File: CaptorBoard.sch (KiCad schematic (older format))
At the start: 55 parts, among them CON1 MINI-USB-SHELD-MC32598, P1 Prog, P2 POWER, P3 EXT, Q1 IRLM6402TRPBF, SW1 CST06S08H, U1 PIC32MX795F512H-80I-PT, U2 MRF24J40MA-I-RM, U3 HTU21, U4 MPL115A2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

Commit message: Forgot foot print
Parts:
- U5: footprint pfo:VTX-214-003-105 -> pfo:VTX-214-005-x
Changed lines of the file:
@@
 F 0 "U5" H 9450 10000 50  0000 C CNN
 F 1 "VTX-214-003-105" H 9750 9400 50  0000 C CNN
-F 2 "pfo:VTX-214-003-105" H 10150 9400 50  0001 C CNN
+F 2 "pfo:VTX-214-005-x" H 10150 9400 50  0001 C CNN
 F 3 "DOCUMENTATION" H 10000 10000 50  0001 C CNN
 	1    9850 9700

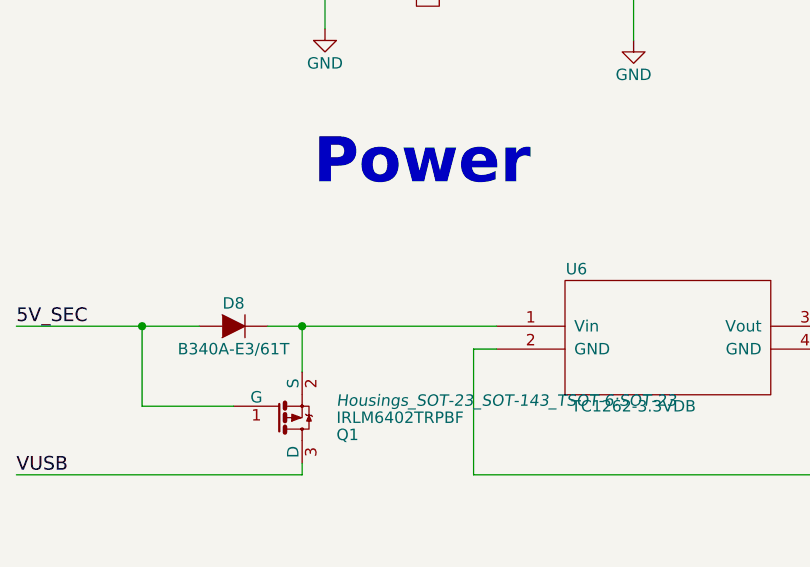
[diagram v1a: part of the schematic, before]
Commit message: Add marker for 5V
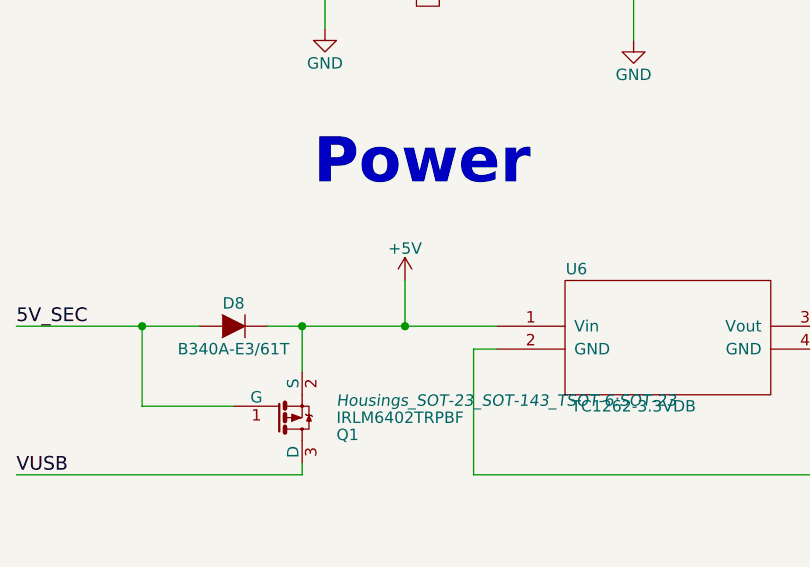
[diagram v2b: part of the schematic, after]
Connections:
- net labels added: +5V
- wire segments 218 -> 219
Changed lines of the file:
@@
 Text Label 12700 7650 0    60   ~ 0
 Phase_F
+$Comp
+L +5V #PWR?
+U 1 1 55364DDB
+P 9600 7750
+F 0 "#PWR?" H 9600 7600 50  0001 C CNN
+F 1 "+5V" H 9600 7890 50  0000 C CNN
+F 2 "" H 9600 7750 60  0000 C CNN
+F 3 "" H 9600 7750 60  0000 C CNN
+	1    9600 7750
+	1    0    0    -1
+$EndComp
+Wire Wire Line
+	9600 7750 9600 7950
+Connection ~ 9600 7950
 $EndSCHEMATC

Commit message: Change HST21
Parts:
- U3: footprint Housings_DFN_QFN:DFN-6-1EP_3x3mm_Pitch0.95mm -> pfo:HTU21
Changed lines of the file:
@@
 F 0 "U3" H 1950 9650 50  0000 C CNN
 F 1 "HTU21" H 2000 9050 50  0000 C CNN
-F 2 "Housings_DFN_QFN:DFN-6-1EP_3x3mm_Pitch0.95mm" H 2650 9050 50  0001 C CNN
+F 2 "pfo:HTU21" H 2650 9050 50  0001 C CNN
 F 3 "DOCUMENTATION" H 2500 9650 50  0001 C CNN
 	1    2350 9350
@@
 Phase_F
 $Comp
-L +5V #PWR?
+L +5V #PWR033
 U 1 1 55364DDB
 P 9600 7750
-F 0 "#PWR?" H 9600 7600 50  0001 C CNN
+F 0 "#PWR033" H 9600 7600 50  0001 C CNN
 F 1 "+5V" H 9600 7890 50  0000 C CNN
 F 2 "" H 9600 7750 60  0000 C CNN

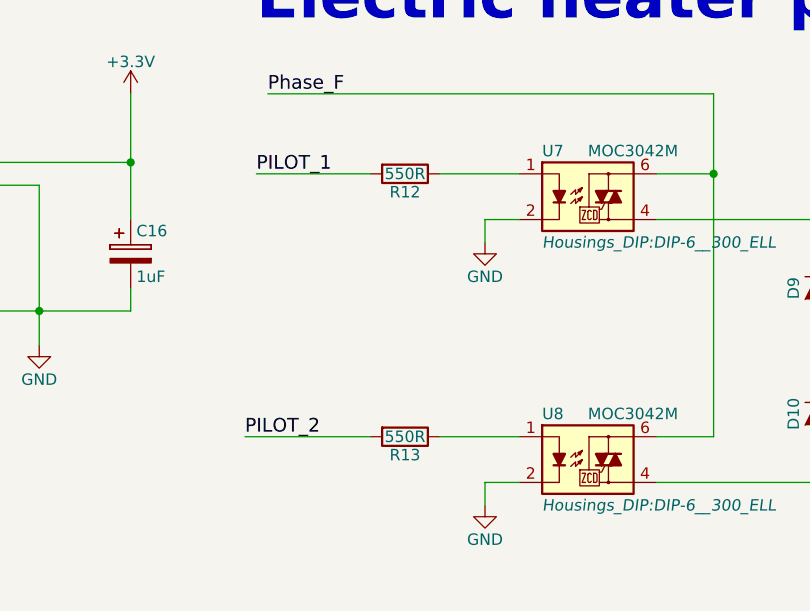
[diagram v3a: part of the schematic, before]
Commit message: Replace Value 550 ohm to 560ohm (mormailsition)
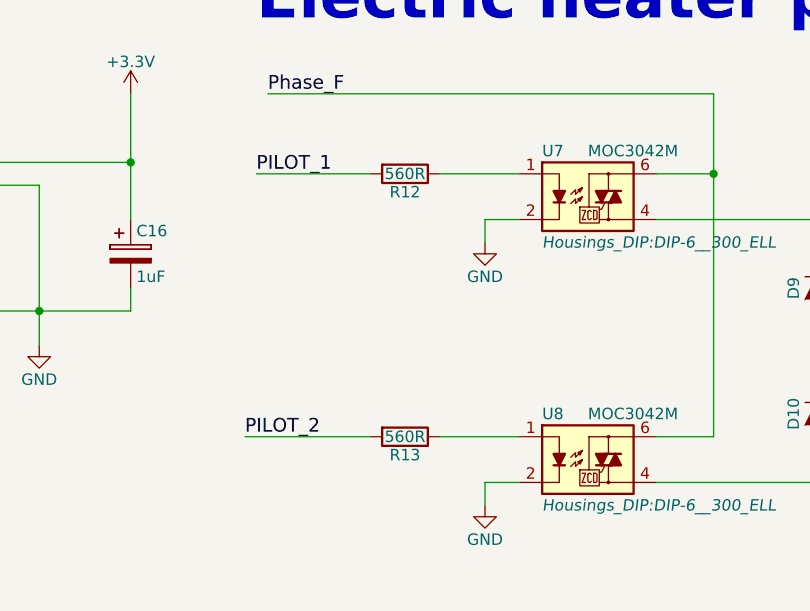
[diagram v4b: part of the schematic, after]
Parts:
- R12, R13: value 550R -> 560R
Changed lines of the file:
@@
 P 13300 8000
 F 0 "R12" V 13380 8000 50  0000 C CNN
-F 1 "550R" V 13300 8000 50  0000 C CNN
+F 1 "560R" V 13300 8000 50  0000 C CNN
 F 2 "Resistors_SMD:R_0805" V 13230 8000 30  0001 C CNN
 F 3 "" H 13300 8000 30  0000 C CNN
@@
 P 13300 9150
 F 0 "R13" V 13380 9150 50  0000 C CNN
-F 1 "550R" V 13300 9150 50  0000 C CNN
+F 1 "560R" V 13300 9150 50  0000 C CNN
 F 2 "Resistors_SMD:R_0805" V 13230 9150 30  0001 C CNN
 F 3 "" H 13300 9150 30  0000 C CNN

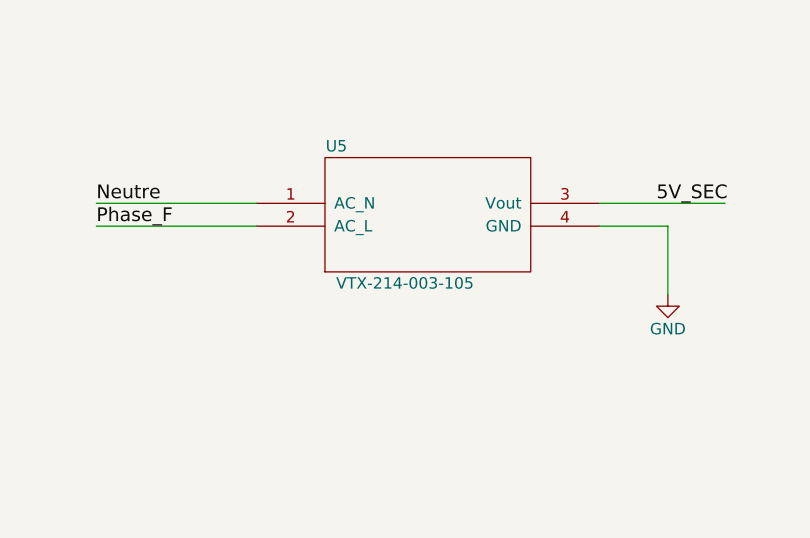
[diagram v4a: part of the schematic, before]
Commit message: Error of ref
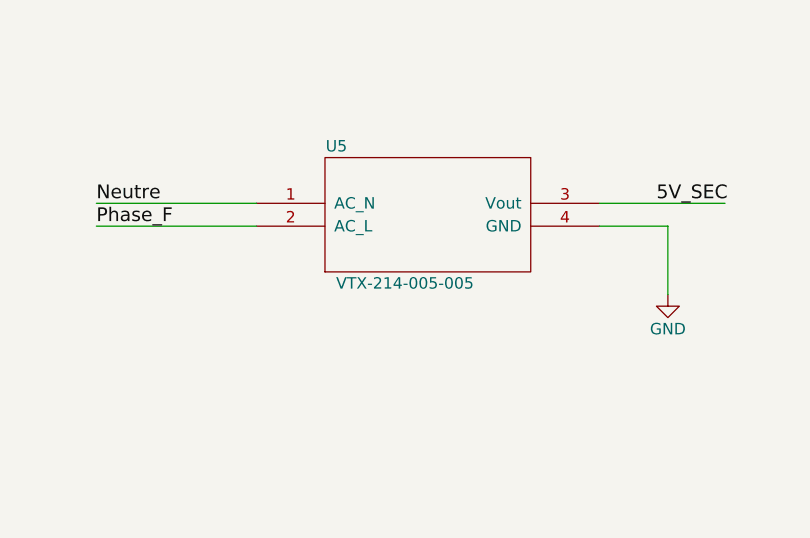
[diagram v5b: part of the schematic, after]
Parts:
- U5: value VTX-214-003-105 -> VTX-214-005-005
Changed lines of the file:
@@
 P 9850 9700
 F 0 "U5" H 9450 10000 50  0000 C CNN
-F 1 "VTX-214-003-105" H 9750 9400 50  0000 C CNN
+F 1 "VTX-214-005-005" H 9750 9400 50  0000 C CNN
 F 2 "pfo:VTX-214-005-x" H 10150 9400 50  0001 C CNN
 F 3 "DOCUMENTATION" H 10000 10000 50  0001 C CNN

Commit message: Change led package to 3mm
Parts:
- D3, D4, D5, D6, D7: footprint pfo:LED-1206-Guide -> LEDs:LED-3MM
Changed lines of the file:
@@
 F 0 "D3" H 6100 8250 50  0000 C CNN
 F 1 "POWER" H 6100 8050 50  0000 C CNN
-F 2 "pfo:LED-1206-Guide" H 6100 8150 60  0001 C CNN
+F 2 "LEDs:LED-3MM" H 6100 8150 60  0001 C CNN
 F 3 "" H 6100 8150 60  0000 C CNN
 	1    6100 8150
@@
 F 0 "D4" H 6100 8600 50  0000 C CNN
 F 1 "CONF" H 6100 8400 50  0000 C CNN
-F 2 "pfo:LED-1206-Guide" H 6100 8500 60  0001 C CNN
+F 2 "LEDs:LED-3MM" H 6100 8500 60  0001 C CNN
 F 3 "" H 6100 8500 60  0000 C CNN
 	1    6100 8500
@@
 F 0 "D5" H 6100 8950 50  0000 C CNN
 F 1 "ECO" H 6100 8750 50  0000 C CNN
-F 2 "pfo:LED-1206-Guide" H 6100 8850 60  0001 C CNN
+F 2 "LEDs:LED-3MM" H 6100 8850 60  0001 C CNN
 F 3 "" H 6100 8850 60  0000 C CNN
 	1    6100 8850
@@
 F 0 "D6" H 6100 9300 50  0000 C CNN
 F 1 "CONF-1°C" H 6100 9100 50  0000 C CNN
-F 2 "pfo:LED-1206-Guide" H 6100 9200 60  0001 C CNN
+F 2 "LEDs:LED-3MM" H 6100 9200 60  0001 C CNN
 F 3 "" H 6100 9200 60  0000 C CNN
 	1    6100 9200
@@
 F 0 "D7" H 6100 9650 50  0000 C CNN
 F 1 "CONF-2°C" H 6100 9450 50  0000 C CNN
-F 2 "pfo:LED-1206-Guide" H 6100 9550 60  0001 C CNN
+F 2 "LEDs:LED-3MM" H 6100 9550 60  0001 C CNN
 F 3 "" H 6100 9550 60  0000 C CNN
 	1    6100 9550

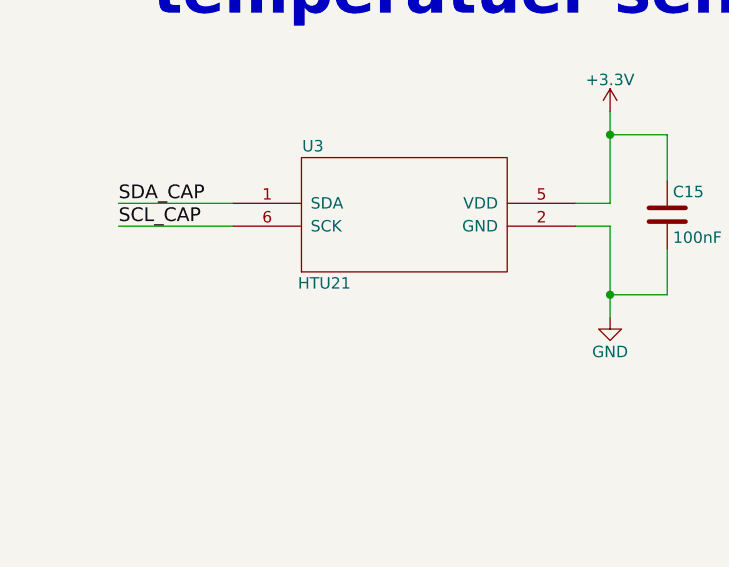
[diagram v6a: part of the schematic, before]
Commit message: Change RH/temp sensor to STH21
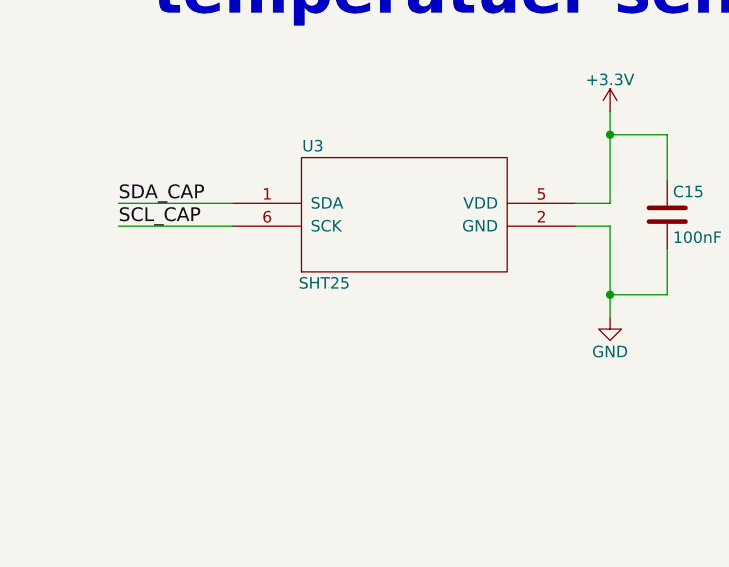
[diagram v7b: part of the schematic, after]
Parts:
- U3: value HTU21 -> SHT25
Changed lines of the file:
@@
 P 2350 9350
 F 0 "U3" H 1950 9650 50  0000 C CNN
-F 1 "HTU21" H 2000 9050 50  0000 C CNN
+F 1 "SHT25" H 2000 9050 50  0000 C CNN
 F 2 "pfo:HTU21" H 2650 9050 50  0001 C CNN
 F 3 "DOCUMENTATION" H 2500 9650 50  0001 C CNN

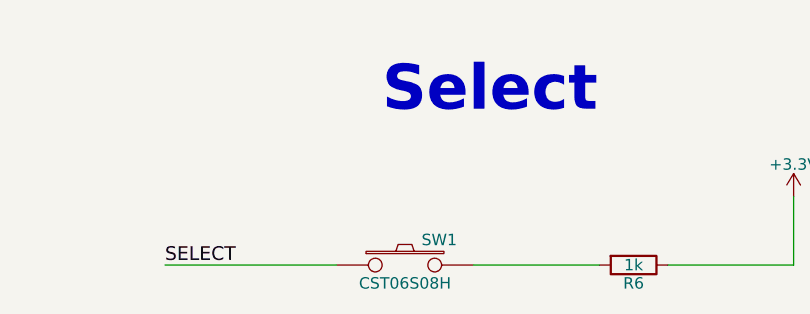
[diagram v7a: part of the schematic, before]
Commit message: Change Button ref
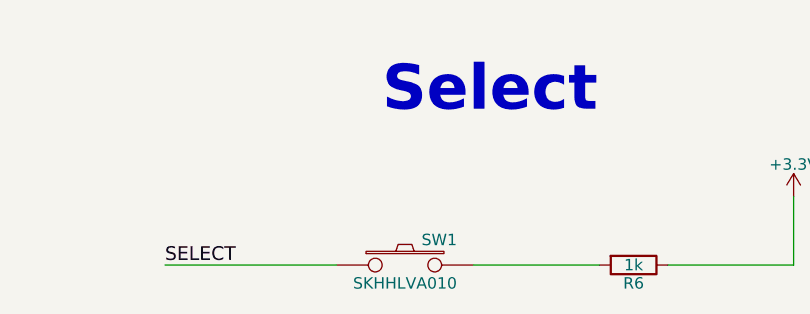
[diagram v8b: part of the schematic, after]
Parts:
- SW1: value CST06S08H -> SKHHLVA010
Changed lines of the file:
@@
 P 5800 10900
 F 0 "SW1" H 5950 11010 50  0000 C CNN
-F 1 "CST06S08H" H 5800 10820 50  0000 C CNN
+F 1 "SKHHLVA010" H 5800 10820 50  0000 C CNN
 F 2 "pfo:CST06S" H 5800 10900 60  0001 C CNN
 F 3 "" H 5800 10900 60  0000 C CNN
